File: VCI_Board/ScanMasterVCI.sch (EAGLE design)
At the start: 77 parts, among them IC1 XMEGA16A4A, Q13 MMBT3904, Q14 MMBT3904, Q15 MMBT3904, Q2 NDC7002N, Q3 MMBT3904, Q5 NTZD5110N, Q6 MMBT3904, Q7 ZXMP6A17G, Q8 MMBT4403, Q9 NDC7002N, U1 MAX17502FATB+, U2 SN65HVDA195-Q1, U3 MAX17502EATB+, U4 L78L08ABUTR

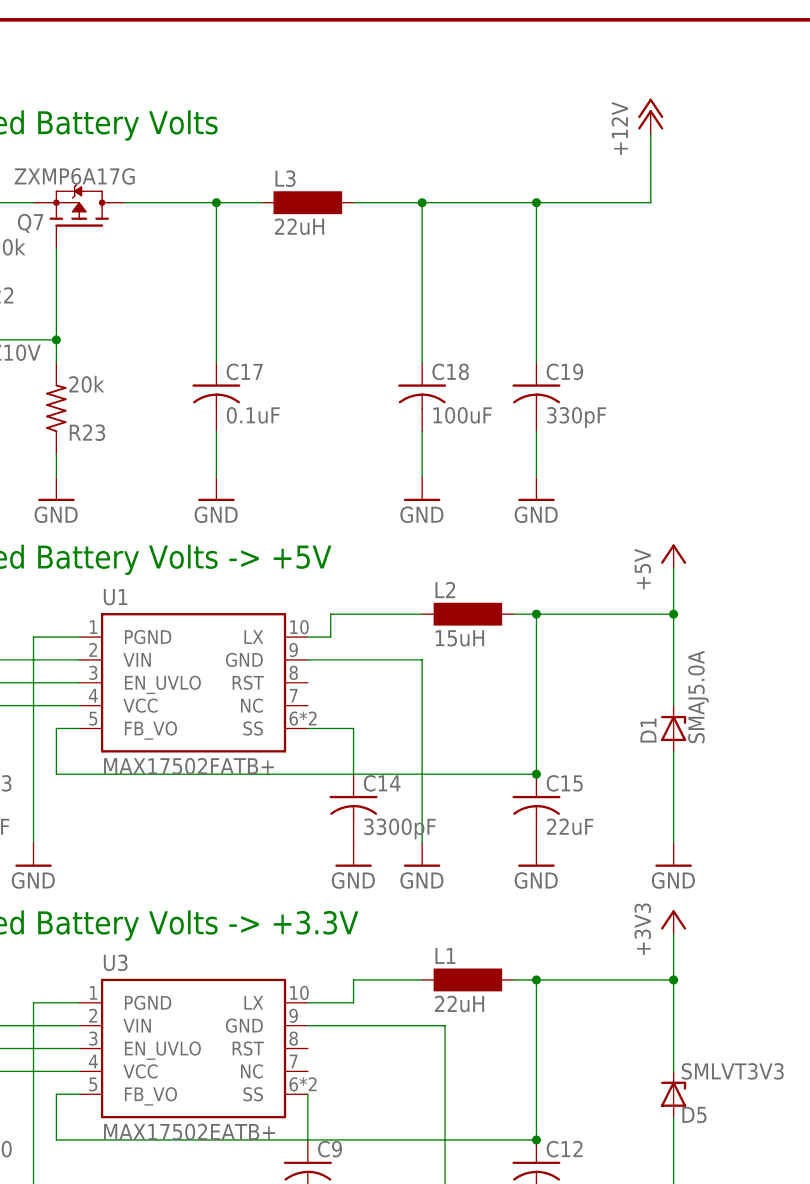
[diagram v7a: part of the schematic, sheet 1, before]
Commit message: Had to change inductors. Inductor package I was using apparently has no basis in reality. Switched it out for a standard 0603.
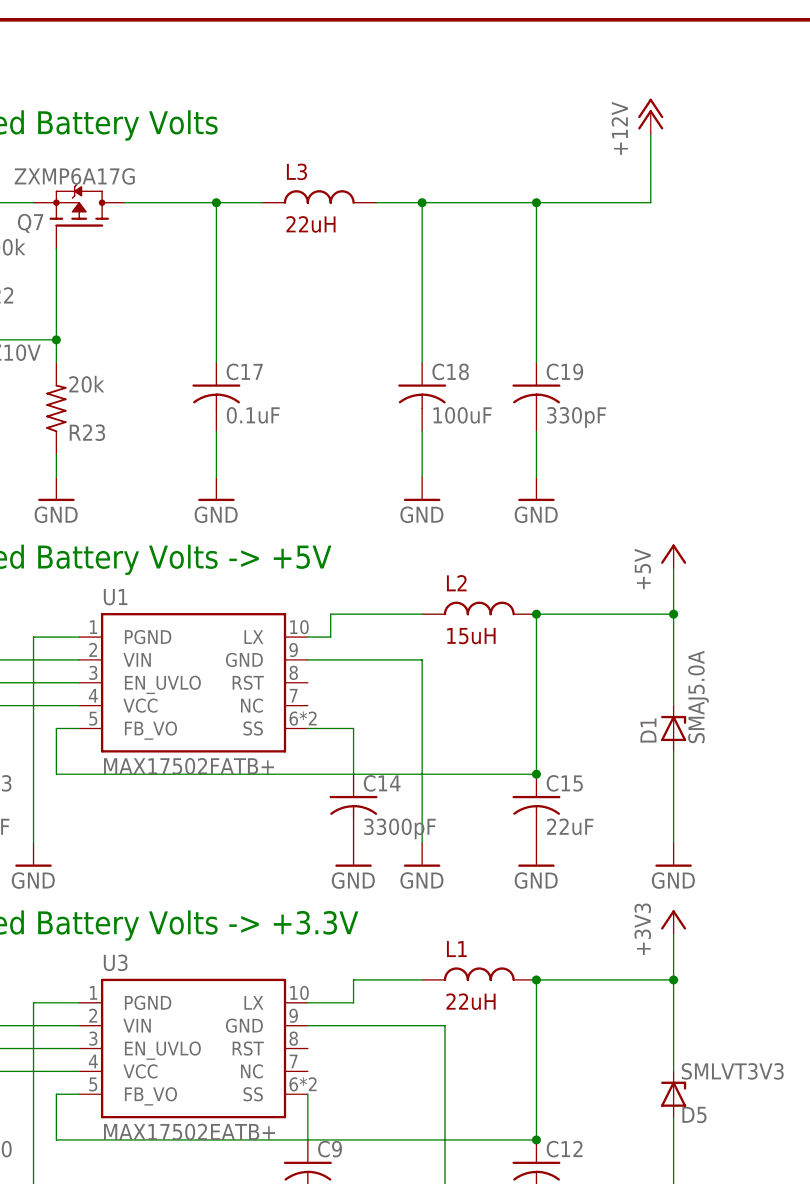
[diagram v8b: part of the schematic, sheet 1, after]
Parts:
- L1, L2, L3: device inductor-neosid:MS50 -> customics:INDUCTOR
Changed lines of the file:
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@@
 <grid distance="0.1" unitdist="inch" unit="inch" style="lines" multiple="1" display="no" altdistance="0.01" altunitdist="inch" altunit="inch"/>
 <layers>
-<layer number="1" name="Top" color="4" fill="1" visible="yes" active="no"/>
-<layer number="16" name="Bottom" color="1" fill="1" visible="yes" active="no"/>
-<layer number="17" name="Pads" color="2" fill="1" visible="yes" active="no"/>
-<layer number="18" name="Vias" color="2" fill="1" visible="yes" active="no"/>
-<layer number="19" name="Unrouted" color="6" fill="1" visible="yes" active="no"/>
-<layer number="20" name="Dimension" color="24" fill="1" visible="yes" active="no"/>
-<layer number="21" name="tPlace" color="7" fill="1" visible="yes" active="no"/>
-<layer number="22" name="bPlace" color="7" fill="1" visible="yes" active="no"/>
-<layer number="23" name="tOrigins" color="15" fill="1" visible="yes" active="no"/>
-<layer number="24" name="bOrigins" color="15" fill="1" visible="yes" active="no"/>
-<layer number="25" name="tNames" color="7" fill="1" visible="yes" active="no"/>
-<layer number="26" name="bNames" color="7" fill="1" visible="yes" active="no"/>
-<layer number="27" name="tValues" color="7" fill="1" visible="yes" active="no"/>
-<layer number="28" name="bValues" color="7" fill="1" visible="yes" active="no"/>
+<layer number="1" name="Top" color="4" fill="1" visible="no" active="no"/>
+<layer number="16" name="Bottom" color="1" fill="1" visible="no" active="no"/>
+<layer number="17" name="Pads" color="2" fill="1" visible="no" active="no"/>
+<layer number="18" name="Vias" color="2" fill="1" visible="no" active="no"/>
+<layer number="19" name="Unrouted" color="6" fill="1" visible="no" active="no"/>
+<layer number="20" name="Dimension" color="24" fill="1" visible="no" active="no"/>
+<layer number="21" name="tPlace" color="7" fill="1" visible="no" active="no"/>
+<layer number="22" name="bPlace" color="7" fill="1" visible="no" active="no"/>
+<layer number="23" name="tOrigins" color="15" fill="1" visible="no" active="no"/>
+<layer number="24" name="bOrigins" color="15" fill="1" visible="no" active="no"/>
+<layer number="25" name="tNames" color="7" fill="1" visible="no" active="no"/>
+<layer number="26" name="bNames" color="7" fill="1" visible="no" active="no"/>
+<layer number="27" name="tValues" color="7" fill="1" visible="no" active="no"/>
+<layer number="28" name="bValues" color="7" fill="1" visible="no" active="no"/>
 <layer number="29" name="tStop" color="7" fill="3" visible="no" active="no"/>
 <layer number="30" name="bStop" color="7" fill="6" visible="no" active="no"/>
@@
 <layer number="35" name="tGlue" color="7" fill="4" visible="no" active="no"/>
 <layer number="36" name="bGlue" color="7" fill="5" visible="no" active="no"/>
-<layer number="37" name="tTest" color="7" fill="1" visible="yes" active="no"/>
-<layer number="38" name="bTest" color="7" fill="1" visible="yes" active="no"/>
+<layer number="37" name="tTest" color="7" fill="1" visible="no" active="no"/>
+<layer number="38" name="bTest" color="7" fill="1" visible="no" active="no"/>
 <layer number="39" name="tKeepout" color="4" fill="11" visible="no" active="no"/>
 <layer number="40" name="bKeepout" color="1" fill="11" visible="no" active="no"/>
@@
 <layer number="44" name="Drills" color="7" fill="1" visible="no" active="no"/>
 <layer number="45" name="Holes" color="7" fill="1" visible="no" active="no"/>
-<layer number="46" name="Milling" color="3" fill="1" visible="yes" active="no"/>
-<layer number="47" name="Measures" color="7" fill="1" visible="yes" active="no"/>
-<layer number="48" name="Document" color="7" fill="1" visible="yes" active="no"/>
-<layer number="49" name="Reference" color="7" fill="1" visible="yes" active="no"/>
-<layer number="50" name="dxf" color="7" fill="1" visible="yes" active="no"/>
-<layer number="51" name="tDocu" color="7" fill="1" visible="yes" active="no"/>
-<layer number="52" name="bDocu" color="7" fill="1" visible="yes" active="no"/>
-<layer number="53" name="tGND_GNDA" color="7" fill="9" visible="yes" active="no"/>
-<layer number="54" name="bGND_GNDA" color="1" fill="9" visible="yes" active="no"/>
-<layer number="56" name="wert" color="7" fill="1" visible="yes" active="no"/>
-<layer number="57" name="tCAD" color="7" fill="1" visible="yes" active="no"/>
-<layer number="59" name="tCarbon" color="7" fill="1" visible="yes" active="no"/>
-<layer number="60" name="bCarbon" color="7" fill="1" visible="yes" active="no"/>
-<layer number="61" name="stand" color="7" fill="1" visible="yes" active="no"/>
+<layer number="46" name="Milling" color="3" fill="1" visible="no" active="no"/>
+<layer number="47" name="Measures" color="7" fill="1" visible="no" active="no"/>
+<layer number="48" name="Document" color="7" fill="1" visible="no" active="no"/>
+<layer number="49" name="Reference" color="7" fill="1" visible="no" active="no"/>
+<layer number="50" name="dxf" color="7" fill="1" visible="no" active="no"/>
+<layer number="51" name="tDocu" color="7" fill="1" visible="no" active="no"/>
+<layer number="52" name="bDocu" color="7" fill="1" visible="no" active="no"/>
+<layer number="53" name="tGND_GNDA" color="7" fill="9" visible="no" active="no"/>
+<layer number="54" name="bGND_GNDA" color="1" fill="9" visible="no" active="no"/>
+<layer number="56" name="wert" color="7" fill="1" visible="no" active="no"/>
+<layer number="57" name="tCAD" color="7" fill="1" visible="no" active="no"/>
+<layer number="59" name="tCarbon" color="7" fill="1" visible="no" active="no"/>
+<layer number="60" name="bCarbon" color="7" fill="1" visible="no" active="no"/>
+<layer number="61" name="stand" color="7" fill="1" visible="no" active="no"/>
 <layer number="88" name="SimResults" color="9" fill="1" visible="yes" active="yes"/>
 <layer number="89" name="SimProbes" color="9" fill="1" visible="yes" active="yes"/>
@@
 <part name="R9" library="adafruit" library_urn="urn:adsk.eagle:library:420" deviceset="R-US_" device="R0603" value="3.32M"/>
 <part name="P+2" library="supply1" library_urn="urn:adsk.eagle:library:371" deviceset="+12V" device=""/>
-<part name="L1" library="inductor-neosid" library_urn="urn:adsk.eagle:library:241" deviceset="MS50" device="" package3d_urn="urn:adsk.eagle:package:14699/1" value="22uH"/>
+<part name="L1" library="customics" deviceset="INDUCTOR" device="" value="22uH"/>
 <part name="+3V4" library="supply1" library_urn="urn:adsk.eagle:library:371" deviceset="+3V3" device=""/>
 <part name="D5" library="diode" library_urn="urn:adsk.eagle:library:210" deviceset="ZENER-DIODE" device="SMB" package3d_urn="urn:adsk.eagle:package:43404/2" value="SMLVT3V3"/>
@@
 <part name="C14" library="adafruit" library_urn="urn:adsk.eagle:library:420" deviceset="C-US" device="C0603" value="3300pF"/>
 <part name="GND20" library="supply1" library_urn="urn:adsk.eagle:library:371" deviceset="GND" device=""/>
-<part name="L2" library="inductor-neosid" library_urn="urn:adsk.eagle:library:241" deviceset="MS50" device="" package3d_urn="urn:adsk.eagle:package:14699/1" value="15uH"/>
+<part name="L2" library="customics" deviceset="INDUCTOR" device="" value="15uH"/>
 <part name="C15" library="adafruit" library_urn="urn:adsk.eagle:library:420" deviceset="C-US" device="C0603" value="22uF"/>
 <part name="P+9" library="supply1" library_urn="urn:adsk.eagle:library:371" deviceset="+5V" device=""/>
@@
 <part name="R23" library="adafruit" library_urn="urn:adsk.eagle:library:420" deviceset="R-US_" device="R0603" value="20k"/>
 <part name="GND38" library="supply1" library_urn="urn:adsk.eagle:library:371" deviceset="GND" device=""/>
-<part name="L3" library="inductor-neosid" library_urn="urn:adsk.eagle:library:241" deviceset="MS50" device="" package3d_urn="urn:adsk.eagle:package:14699/1" value="22uH"/>
+<part name="L3" library="customics" deviceset="INDUCTOR" device="" value="22uH"/>
 <part name="C17" library="adafruit" library_urn="urn:adsk.eagle:library:420" deviceset="C-US" device="C0603" value="0.1uF"/>
 <part name="GND39" library="supply1" library_urn="urn:adsk.eagle:library:371" deviceset="GND" device=""/>
@@
 <segment>
 <pinref part="L1" gate="G$1" pin="2"/>
-<wire x1="205.74" y1="78.74" x2="208.28" y2="78.74" width="0.1524" layer="91"/>
 <wire x1="208.28" y1="78.74" x2="223.52" y2="78.74" width="0.1524" layer="91"/>
 <wire x1="223.52" y1="78.74" x2="223.52" y2="83.82" width="0.1524" layer="91"/>
@@
 <segment>
 <pinref part="L3" gate="G$1" pin="2"/>
-<wire x1="187.96" y1="165.1" x2="195.58" y2="165.1" width="0.1524" layer="91"/>
+<wire x1="190.5" y1="165.1" x2="195.58" y2="165.1" width="0.1524" layer="91"/>
 <wire x1="195.58" y1="165.1" x2="208.28" y2="165.1" width="0.1524" layer="91"/>
 <wire x1="208.28" y1="165.1" x2="220.98" y2="165.1" width="0.1524" layer="91"/>
@@
 <segment>
 <pinref part="L2" gate="G$1" pin="2"/>
-<wire x1="205.74" y1="119.38" x2="208.28" y2="119.38" width="0.1524" layer="91"/>
 <wire x1="208.28" y1="119.38" x2="223.52" y2="119.38" width="0.1524" layer="91"/>
 <wire x1="223.52" y1="119.38" x2="223.52" y2="124.46" width="0.1524" layer="91"/>
